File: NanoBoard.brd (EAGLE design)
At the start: 100 x 80 mm, 16 parts, among them IC1 ATMEGA32U2-TQFP, Q1 16MHz

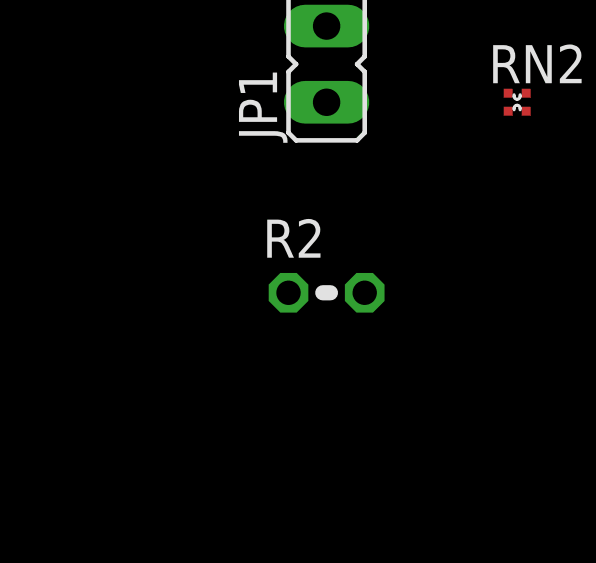
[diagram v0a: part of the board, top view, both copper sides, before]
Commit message: Fixed some errors Eagle discovered, and changed the pins the LED is on because they are analog pins.
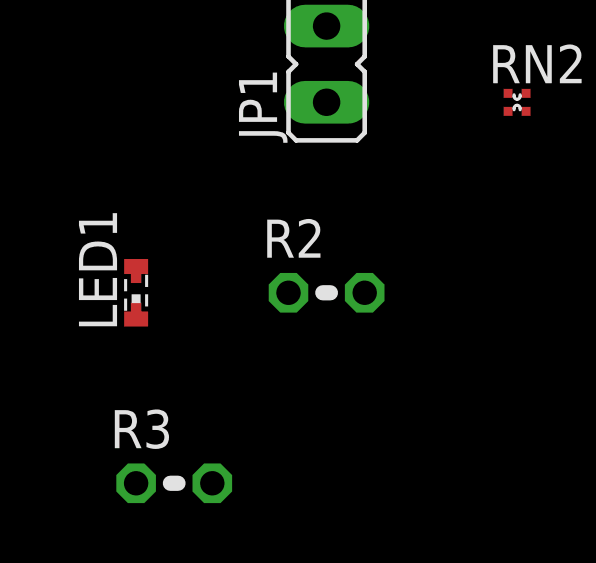
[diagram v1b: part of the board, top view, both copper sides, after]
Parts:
- added LED1: (no value), adafruit:SMARTLED-TTW
- added R3: 120R, resistor:0204V
- R2: value (none) -> 1k
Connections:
- new net +5V: JP1.2
- new net N$12: IC1.15
- new net N$13: IC1.14
- new net N$14: IC1.22, LED1.A@1
- new net N$15: LED1.C@1, R3.1
- new net N$5: C4.2, IC1.27
- new net SPI_MASTER_OUTPUT: IC1.16
- net GND: now also R3.2
- net N$1: now also X1.1
- net N$10: now also IC1.28
- net N$11: now also IC1.5, JP1.1; no longer IC1.13
- net N$2: now also X1.2
- net N$6: now also IC1.30
- net N$7: now also IC1.29
- net N$8: now also IC1.1
- net N$9: now also C2.2, IC1.2
- net RX: now also IC1.8
- net TX: now also IC1.9
- net USBVCC: now also IC1.4
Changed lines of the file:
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@@
 </element>
 <element name="JP1" library="jumper" package="JP1" value="" x="-30.48" y="-74.93"/>
-<element name="R2" library="resistor" package="0204V" value="" x="-30.48" y="-82.55"/>
+<element name="R2" library="resistor" package="0204V" value="1k" x="-30.48" y="-82.55"/>
+<element name="LED1" library="adafruit" package="SMARTLED-TTW" value="" x="-36.83" y="-82.55"/>
+<element name="R3" library="resistor" package="0204V" value="120R" x="-35.56" y="-88.9"/>
 </elements>
 <signals>
 <signal name="N$1">
 <contactref element="F1" pad="2"/>
+<contactref element="X1" pad="1"/>
+<wire x1="-7.64" y1="16.14" x2="-10.75" y2="-3.81" width="0" layer="19" extent="1-1"/>
 </signal>
 <signal name="USBVCC">
@@
 <contactref element="IC1" pad="32"/>
 <contactref element="C3" pad="1"/>
-<wire x1="-24.39" y1="-19.8374" x2="-25.4" y2="-62.23" width="0" layer="19" extent="1-1"/>
+<contactref element="IC1" pad="4"/>
+<wire x1="-25.8826" y1="-23.73" x2="-25.4" y2="-62.23" width="0" layer="19" extent="1-1"/>
+<wire x1="-24.39" y1="-19.8374" x2="-25.8826" y2="-23.73" width="0" layer="19" extent="1-1"/>
 <wire x1="-23.59" y1="-19.8374" x2="-24.39" y2="-19.8374" width="0" layer="19" extent="1-1"/>
 <wire x1="-14.65" y1="-3.81" x2="-23.59" y2="-19.8374" width="0" layer="19" extent="1-1"/>
@@
 <contactref element="RN1" pad="8"/>
 <contactref element="Z2" pad="1"/>
+<contactref element="X1" pad="2"/>
 <wire x1="-13.9" y1="-10.755" x2="-14.97" y2="-22.86" width="0" layer="19" extent="1-1"/>
+<wire x1="-10.14" y1="16.14" x2="-13.9" y2="-10.755" width="0" layer="19" extent="1-1"/>
 </signal>
 <signal name="N$3">
@@
 <signal name="N$6">
 <contactref element="RN1" pad="1"/>
+<contactref element="IC1" pad="30"/>
+<wire x1="-13.9" y1="-12.105" x2="-22.79" y2="-19.8374" width="0" layer="19" extent="1-1"/>
 </signal>
 <signal name="N$7">
 <contactref element="RN1" pad="4"/>
+<contactref element="IC1" pad="29"/>
+<wire x1="-11.5" y1="-12.105" x2="-21.99" y2="-19.8374" width="0" layer="19" extent="1-1"/>
 </signal>
 <signal name="N$8">
@@
 <contactref element="Q1" pad="1"/>
 <contactref element="C1" pad="2"/>
+<contactref element="IC1" pad="1"/>
 <wire x1="-22.86" y1="-40.64" x2="-22.86" y2="-49.53" width="0" layer="19" extent="1-1"/>
 <wire x1="-23.28" y1="-33.02" x2="-22.86" y2="-40.64" width="0" layer="19" extent="1-1"/>
+<wire x1="-25.8826" y1="-21.33" x2="-23.28" y2="-33.02" width="0" layer="19" extent="1-1"/>
 </signal>
 <signal name="N$9">
 <contactref element="R1" pad="1"/>
 <contactref element="Q1" pad="2"/>
+<contactref element="IC1" pad="2"/>
+<contactref element="C2" pad="2"/>
+<wire x1="-17.78" y1="-40.64" x2="-22.86" y2="-54.61" width="0" layer="19" extent="1-1"/>
 <wire x1="-24.98" y1="-33.02" x2="-17.78" y2="-40.64" width="0" layer="19" extent="1-1"/>
+<wire x1="-25.8826" y1="-22.13" x2="-24.98" y2="-33.02" width="0" layer="19" extent="1-1"/>
 </signal>
 <signal name="N$10">
@@
 <contactref element="L1" pad="1"/>
 <contactref element="C4" pad="1"/>
+<contactref element="IC1" pad="28"/>
 <wire x1="-25.4" y1="-54.61" x2="-25.4" y2="-69.85" width="0" layer="19" extent="1-1"/>
 <wire x1="-25.4" y1="-49.53" x2="-25.4" y2="-54.61" width="0" layer="19" extent="1-1"/>
 <wire x1="-15.02" y1="-27.94" x2="-25.4" y2="-49.53" width="0" layer="19" extent="1-1"/>
-<wire x1="-25.8826" y1="-22.93" x2="-15.02" y2="-27.94" width="0" layer="19" extent="1-1"/>
-<wire x1="-7.64" y1="14.14" x2="-25.8826" y2="-22.93" width="0" layer="19" extent="1-1"/>
+<wire x1="-21.19" y1="-19.8374" x2="-15.02" y2="-27.94" width="0" layer="19" extent="1-1"/>
+<wire x1="-25.8826" y1="-22.93" x2="-21.19" y2="-19.8374" width="0" layer="19" extent="1-1"/>
+<wire x1="-7.64" y1="14.14" x2="-21.19" y2="-19.8374" width="0" layer="19" extent="1-1"/>
 </signal>
 <signal name="GND">
 <contactref element="C3" pad="2"/>
 <contactref element="R2" pad="2"/>
+<contactref element="R3" pad="2"/>
+<wire x1="-29.21" y1="-82.55" x2="-34.29" y2="-88.9" width="0" layer="19" extent="1-1"/>
 <wire x1="-22.86" y1="-62.23" x2="-29.21" y2="-82.55" width="0" layer="19" extent="1-1"/>
 </signal>
@@
 <signal name="TX">
 <contactref element="RN2" pad="2"/>
+<contactref element="IC1" pad="9"/>
+<wire x1="-24.39" y1="-28.4226" x2="-23.83" y2="-76.5" width="0" layer="19" extent="1-1"/>
 </signal>
 <signal name="RX">
 <contactref element="RN2" pad="1"/>
+<contactref element="IC1" pad="8"/>
+<wire x1="-25.8826" y1="-26.93" x2="-24.43" y2="-76.5" width="0" layer="19" extent="1-1"/>
 </signal>
 <signal name="N$11">
-<contactref element="IC1" pad="13"/>
 <contactref element="R2" pad="1"/>
-<wire x1="-21.19" y1="-28.4226" x2="-31.75" y2="-82.55" width="0" layer="19" extent="1-1"/>
+<contactref element="JP1" pad="1"/>
+<contactref element="IC1" pad="5"/>
+<wire x1="-30.48" y1="-76.2" x2="-31.75" y2="-82.55" width="0" layer="19" extent="1-1"/>
+<wire x1="-25.8826" y1="-24.53" x2="-30.48" y2="-76.2" width="0" layer="19" extent="1-1"/>
+</signal>
+<signal name="N$5">
+<contactref element="C4" pad="2"/>
+<contactref element="IC1" pad="27"/>
+<wire x1="-20.39" y1="-19.8374" x2="-22.86" y2="-69.85" width="0" layer="19" extent="1-1"/>
+</signal>
+<signal name="SPI_MASTER_OUTPUT">
+<contactref element="IC1" pad="16"/>
+</signal>
+<signal name="N$12">
+<contactref element="IC1" pad="15"/>
+</signal>
+<signal name="N$13">
+<contactref element="IC1" pad="14"/>
+</signal>
+<signal name="+5V">
+<contactref element="JP1" pad="2"/>
+</signal>
+<signal name="N$15">
+<contactref element="LED1" pad="C@1"/>
+<contactref element="R3" pad="1"/>
+<wire x1="-36.83" y1="-82.05" x2="-36.83" y2="-88.9" width="0" layer="19" extent="1-1"/>
+</signal>
+<signal name="N$14">
+<contactref element="IC1" pad="22"/>
+<contactref element="LED1" pad="A@1"/>
+<wire x1="-17.2974" y1="-22.93" x2="-36.83" y2="-83.05" width="0" layer="19" extent="1-1"/>
 </signal>
 </signals>
